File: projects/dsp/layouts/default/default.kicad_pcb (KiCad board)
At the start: 4 copper layers, 359 x 72.9 mm, 319 parts

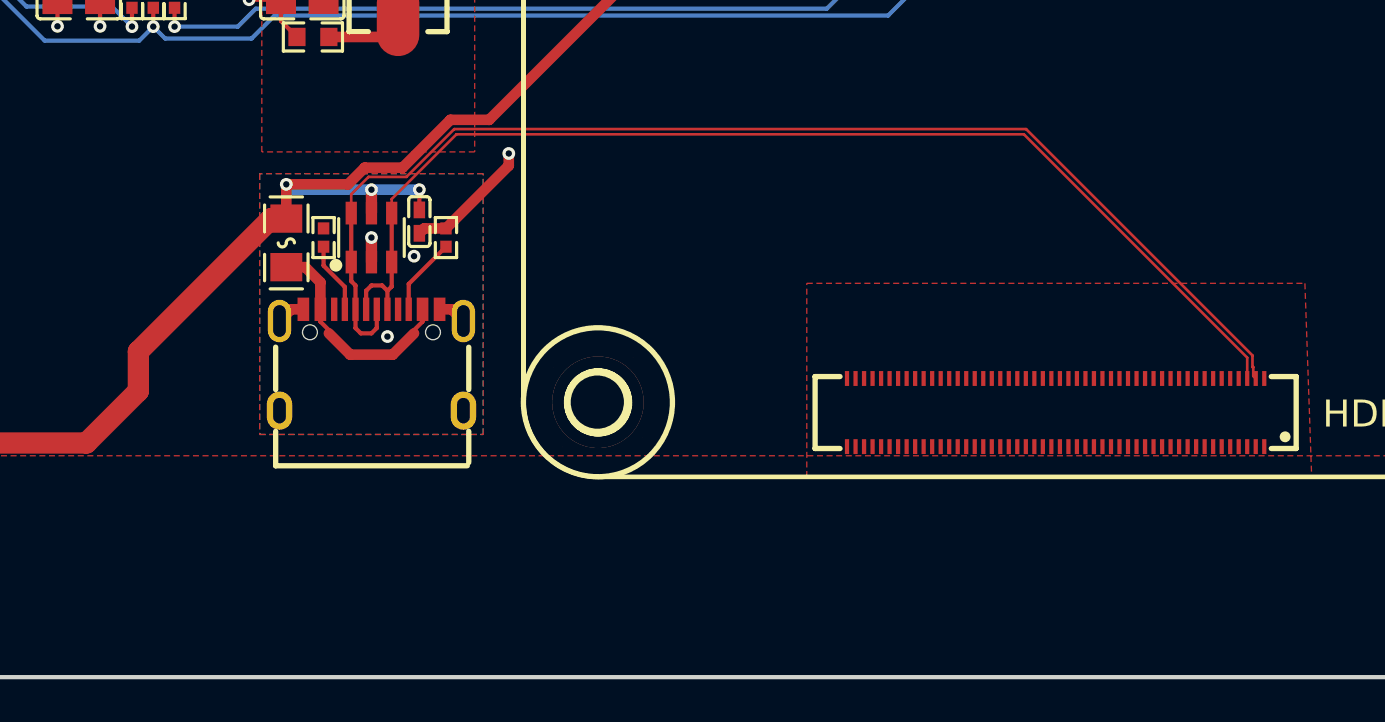
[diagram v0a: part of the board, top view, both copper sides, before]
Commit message: fix all f a b r y k _ c o n v e r t errors in parts
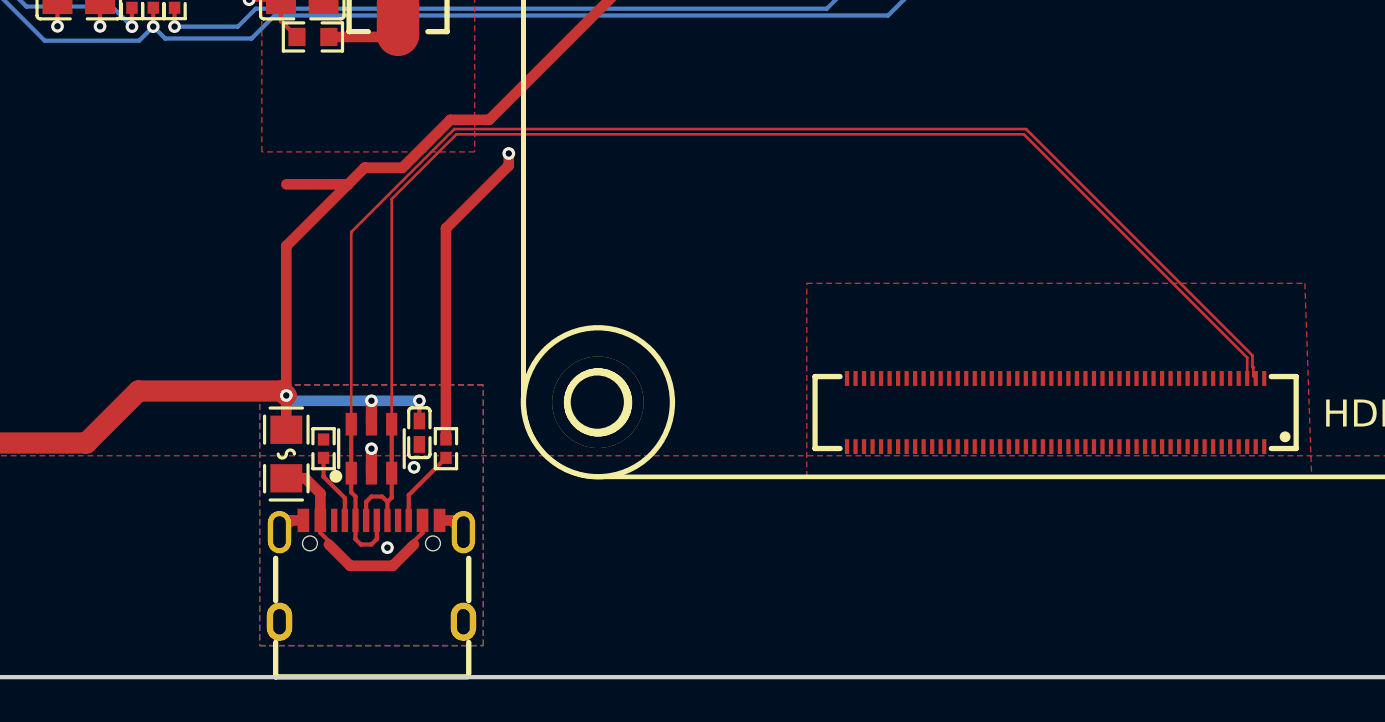
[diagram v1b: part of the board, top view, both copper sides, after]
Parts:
- moved C100 9.92 mm to (259.1, 160.4)
- moved D3 9.92 mm to (256.9, 161.2)
- moved F1 9.92 mm to (252.8, 161.4)
- moved R65 9.92 mm to (254.6, 161.2)
- moved R66 9.92 mm to (260.4, 161.2)
- moved USB1 9.92 mm to (256.9, 166.9)
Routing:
- net power_18v_neg: track 115.2 -> 156.9 mm
- net usb-USB_D_P: track 54.1 -> 64.0 mm
- net usb-USB_D_N: track 57.6 -> 66.5 mm
- net GND: track 412.6 -> 421.2 mm
- net power_5v: track 227.2 -> 234.0 mm

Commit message: repour after build
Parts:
- added LOGO1: , atopile_Logo_25x6mm:atopile_Logo_25x6mm, F.Cu at (357.8, 161.1)
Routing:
- added copper zone on F.Cu, net dsp-net
